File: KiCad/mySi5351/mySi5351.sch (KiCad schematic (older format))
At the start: 51 parts, among them J1 Conn_Coaxial, J2 Conn_Coaxial, J3 Conn_Coaxial, J4 Conn_Coaxial, J5 Conn_01x04_Female, J6 Conn_01x07_Female, J7 Conn_01x01_Female, J8 Conn_Coaxial, J9 Conn_01x02_Female, U1 LM4030-4.096, U2 LM7805_TO220, U3 74132

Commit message: Adds manual routes to pcb
via grid and rounded traces looking well now
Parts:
- added J10: Conn_01x01_Female, Connector_PinHeader_2.54mm:PinHeader_1x02_P2.54mm_Vertical, symbol Connector:Conn_01x02_Female
- added U4: 74HC04, Package_SO:SO-14_3.9x8.65mm_P1.27mm, symbol 74xx:74LS04
- C2, C6: value 22pF -> 27pF
- J9: renamed from J5; value Conn_01x04_Female -> Conn_01x05_Female; footprint Connector_PinHeader_2.54mm:PinHeader_1x04_P2.54mm_Vertical -> Connector_PinHeader_2.54mm:PinHeader_1x05_P2.54mm_Vertical; symbol Connector:Conn_01x04_Female -> Connector:Conn_01x05_Female
- L2: value 62nH -> 82nH
- U2: renamed from U3; value 74132 -> 74HC132; footprint Package_SO:SO-14_5.3x10.2mm_P1.27mm -> Package_SO:SO-14_3.9x8.65mm_P1.27mm
- renumbered C12 to C10, C10 to C11, C11 to C12, J6 to J5, J8 to J6, J9 to J8, U2 to U3
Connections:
- wire segments 125 -> 130
- no-connect marks 25 -> 29
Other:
- note added: "116 MHz"
- note added: "GPSDO Input\n10 MHz"
- note removed: "144 MHz"
- note removed: "GPSDO"
- note removed: "In"
- moved on the sheet: C10, C14, C9, D1, J5, J6, J7, R13, R14, R15, R16, R17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

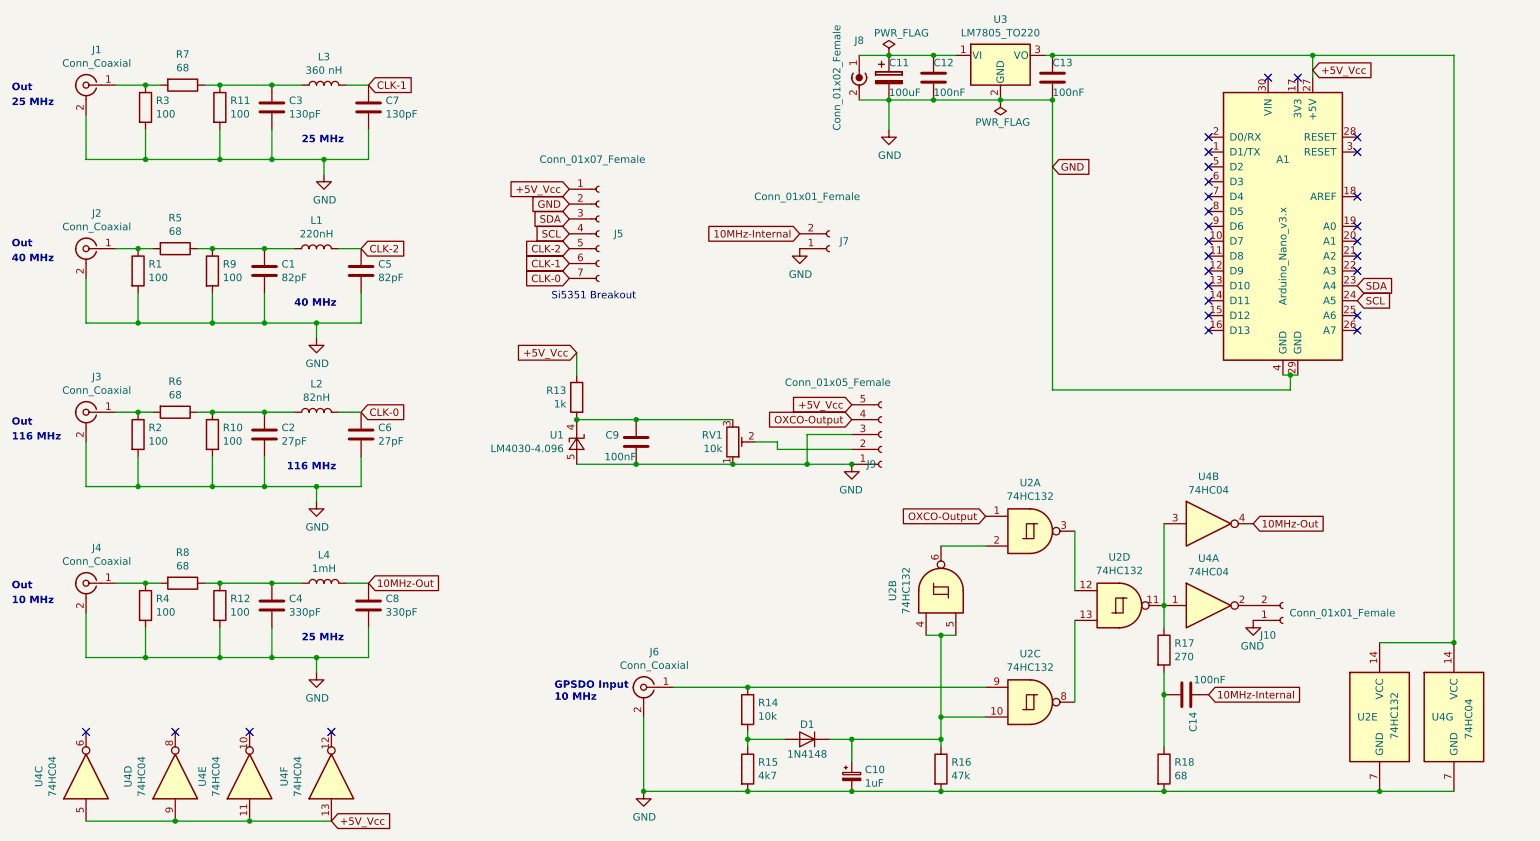
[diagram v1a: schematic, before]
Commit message: Review, plotted files for first useable pcb
The plots are products and send to factory, not included in repo
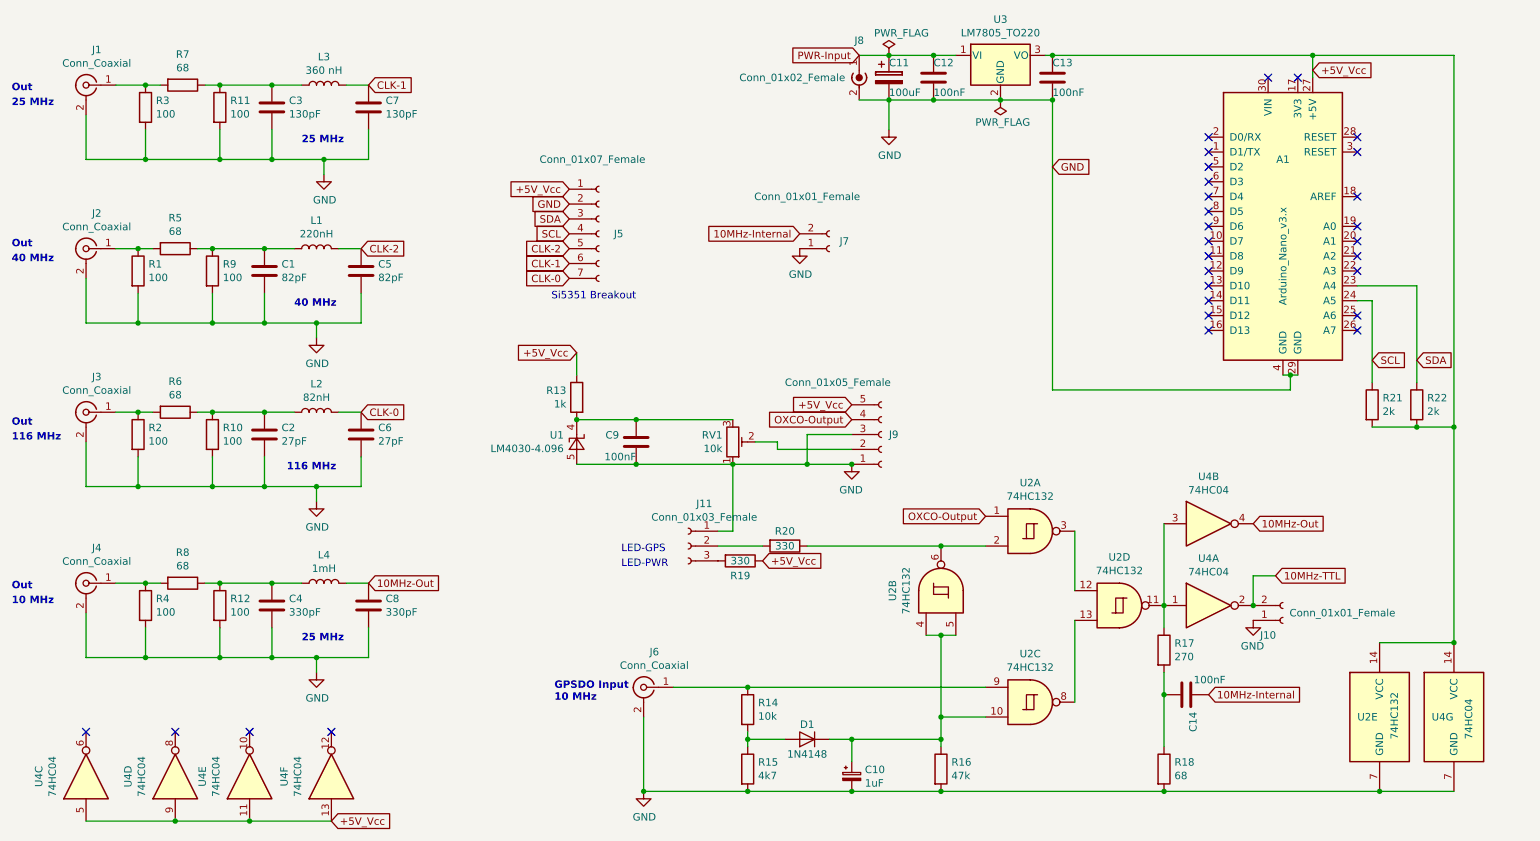
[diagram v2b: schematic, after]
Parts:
- added J11: Conn_01x03_Female, Connector_PinHeader_2.54mm:PinHeader_1x03_P2.54mm_Vertical, symbol Connector:Conn_01x03_Female
- added R19, R20: 330, Resistor_SMD:R_1210_3225Metric_Pad1.30x2.65mm_HandSolder, symbol Device:R
- added R21, R22: 2k, Resistor_SMD:R_1210_3225Metric_Pad1.30x2.65mm_HandSolder, symbol Device:R
- A1: footprint Module:Arduino_Nano -> Module:Arduino_Nano_WithMountingHoles
- C11: footprint Capacitor_SMD:C_3640_9110Metric_Pad2.10x10.45mm_HandSolder -> Capacitor_SMD:CP_Elec_8x10.5
- U3: footprint Package_TO_SOT_THT:TO-220-3_Vertical -> Package_TO_SOT_THT:TO-220-3_Horizontal_TabDown
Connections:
- net +5V_Vcc: now also R19.1, R21.2, R22.2
- net GND: now also J11.1 (Pin_1)
- net SCL: now also R21.1
- net SDA: now also R22.1
- net PWR-Input: now reaches C11.1, C12.1, J8.1 (In), U3.1 (VI)
- net at U2.2, U2.6: now also R20.1
- net 10MHz-TTL: now reaches J10.2 (Pin_2), U4.2
- new net: J11.2 (Pin_2), R20.2
- new net: J11.3 (Pin_3), R19.2
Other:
- note added: "LED-GPS"
- note added: "LED-PWR"
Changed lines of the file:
@@
 Sheet 1 1
 Title "Eurocard-Si5351"
-Date "2020-10-14"
+Date "2020-10-29"
 Rev "v0.1"
 Comp "DO1SLO"
@@
 F 0 "C11" H 6650 1300 50  0000 L CNN
 F 1 "100uF" H 6650 1100 50  0000 L CNN
-F 2 "Capacitor_SMD:C_3640_9110Metric_Pad2.10x10.45mm_HandSolder" H 6688 1050 50  0001 C CNN
+F 2 "Capacitor_SMD:CP_Elec_8x10.5" H 6688 1050 50  0001 C CNN
 F 3 "~" H 6650 1200 50  0001 C CNN
 	1    6650 1200
@@
 P 6450 1150
 F 0 "J8" H 6450 1350 50  0000 C CNN
-F 1 "Conn_01x02_Female" V 6300 1100 50  0000 C CNN
+F 1 "Conn_01x02_Female" H 6000 1100 50  0000 C CNN
 F 2 "Connector_BarrelJack:BarrelJack_Horizontal" H 6450 1150 50  0001 C CNN
 F 3 "~" H 6450 1150 50  0001 C CNN
@@
 U 1 1 5FA061DF
 P 6600 3600
-F 0 "J9" H 6500 3800 50  0000 L CNN
+F 0 "J9" H 6650 3600 50  0000 L CNN
 F 1 "Conn_01x05_Female" H 5950 3250 50  0000 L CNN
 F 2 "Connector_PinHeader_2.54mm:PinHeader_1x05_P2.54mm_Vertical" H 6600 3600 50  0001 C CNN
@@
 F 0 "U3" H 7400 1292 50  0000 C CNN
 F 1 "LM7805_TO220" H 7400 1201 50  0000 C CNN
-F 2 "Package_TO_SOT_THT:TO-220-3_Vertical" H 7400 1275 50  0001 C CIN
+F 2 "Package_TO_SOT_THT:TO-220-3_Horizontal_TabDown" H 7400 1275 50  0001 C CIN
 F 3 "https://www.onsemi.cn/PowerSolutions/document/MC7800-D.PDF" H 7400 1000 50  0001 C CNN
 	1    7400 1050
@@
 F 0 "A1" H 9300 2650 50  0000 C CNN
 F 1 "Arduino_Nano_v3.x" V 9300 2000 50  0000 C CNN
-F 2 "Module:Arduino_Nano" H 9300 2200 50  0001 C CIN
+F 2 "Module:Arduino_Nano_WithMountingHoles" H 9300 2200 50  0001 C CIN
 F 3 "http://www.mouser.com/pdfdocs/Gravitech_Arduino_Nano3_0.pdf" H 9300 2200 50  0001 C CNN
 	1    9300 2200
@@
 NoConn ~ 9800 2200
 NoConn ~ 9800 2300
-Text GLabel 9800 2700 2    50   Input ~ 0
+Text GLabel 9900 3100 2    50   Input ~ 0
 SCL
-Text GLabel 9800 2600 2    50   Input ~ 0
+Text GLabel 10200 3100 2    50   Input ~ 0
 SDA
 NoConn ~ 9800 2400
@@
 	8500 4750 8500 4200
 Wire Wire Line
-	10450 1050 10450 5000
+	10450 1050 10450 3550
 Connection ~ 10450 5000
 $Comp
@@
 Text GLabel 6400 3400 0    50   Input ~ 0
 +5V_Vcc
+Text GLabel 6450 1050 0    50   Input ~ 0
+PWR-Input
+Text GLabel 9250 4550 2    50   Input ~ 0
+10MHz-TTL
+Wire Wire Line
+	9100 4750 9100 4550
+Wire Wire Line
+	9100 4550 9250 4550
+Connection ~ 9100 4750
+$Comp
+L Connector:Conn_01x03_Female J11
+U 1 1 5FA09C1C
+P 5300 4350
+F 0 "J11" H 5192 4635 50  0000 C CNN
+F 1 "Conn_01x03_Female" H 5192 4544 50  0000 C CNN
+F 2 "Connector_PinHeader_2.54mm:PinHeader_1x03_P2.54mm_Vertical" H 5300 4350 50  0001 C CNN
+F 3 "~" H 5300 4350 50  0001 C CNN
+	1    5300 4350
+	-1   0    0    -1
+$EndComp
+$Comp
+L Device:R R20
+U 1 1 5FA0BFB6
+P 5950 4350
+F 0 "R20" V 5850 4350 50  0000 C CNN
+F 1 "330" V 5950 4350 50  0000 C CNN
+F 2 "Resistor_SMD:R_1210_3225Metric_Pad1.30x2.65mm_HandSolder" V 5880 4350 50  0001 C CNN
+F 3 "~" H 5950 4350 50  0001 C CNN
+	1    5950 4350
+	0    1    1    0
+$EndComp
+Wire Wire Line
+	5500 4250 5600 4250
+Wire Wire Line
+	5600 4250 5600 3800
+$Comp
+L Device:R R19
+U 1 1 5FABB847
+P 5650 4450
+F 0 "R19" V 5750 4450 50  0000 C CNN
+F 1 "330" V 5650 4450 50  0000 C CNN
+F 2 "Resistor_SMD:R_1210_3225Metric_Pad1.30x2.65mm_HandSolder" V 5580 4450 50  0001 C CNN
+F 3 "~" H 5650 4450 50  0001 C CNN
+	1    5650 4450
+	0    1    1    0
+$EndComp
+Text GLabel 5800 4450 2    50   Input ~ 0
++5V_Vcc
+Wire Wire Line
+	6100 4350 7000 4350
+Connection ~ 7000 4350
+Wire Wire Line
+	5500 4350 5800 4350
+Text Notes 4850 4400 0    50   ~ 0
+LED-GPS
+Text Notes 4850 4500 0    50   ~ 0
+LED-PWR
+$Comp
+L Device:R R21
+U 1 1 5FB27C97
+P 9900 3400
+F 0 "R21" H 9970 3446 50  0000 L CNN
+F 1 "2k" H 9970 3355 50  0000 L CNN
+F 2 "Resistor_SMD:R_1210_3225Metric_Pad1.30x2.65mm_HandSolder" V 9830 3400 50  0001 C CNN
+F 3 "~" H 9900 3400 50  0001 C CNN
+	1    9900 3400
+	1    0    0    -1
+$EndComp
+$Comp
+L Device:R R22
+U 1 1 5FB28BAD
+P 10200 3400
+F 0 "R22" H 10270 3446 50  0000 L CNN
+F 1 "2k" H 10270 3355 50  0000 L CNN
+F 2 "Resistor_SMD:R_1210_3225Metric_Pad1.30x2.65mm_HandSolder" V 10130 3400 50  0001 C CNN
+F 3 "~" H 10200 3400 50  0001 C CNN
+	1    10200 3400
+	1    0    0    -1
+$EndComp
+Wire Wire Line
+	9800 2700 9900 2700
+Wire Wire Line
+	9900 2700 9900 3250
+Connection ~ 10450 3550
+Wire Wire Line
+	10450 3550 10450 5000
+Wire Wire Line
+	10200 3550 10450 3550
+Wire Wire Line
+	9900 3550 10200 3550
+Connection ~ 10200 3550
+Wire Wire Line
+	9800 2600 10200 2600
+Wire Wire Line
+	10200 2600 10200 3250
 $EndSCHEMATC

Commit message: Fixed a bug in schema, 100 instead of 10k Ohms
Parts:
- R14: value 10k -> 100
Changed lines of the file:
@@
 EESchema Schematic File Version 4
-EELAYER 30 0
+LIBS:mySi5351-cache
+EELAYER 26 0
 EELAYER END
 $Descr A4 11693 8268
@@
 P 5700 5450
 F 0 "R14" H 5770 5496 50  0000 L CNN
-F 1 "10k" H 5770 5405 50  0000 L CNN
+F 1 "100" H 5770 5405 50  0000 L CNN
 F 2 "Resistor_SMD:R_1210_3225Metric_Pad1.30x2.65mm_HandSolder" V 5630 5450 50  0001 C CNN
 F 3 "~" H 5700 5450 50  0001 C CNN
